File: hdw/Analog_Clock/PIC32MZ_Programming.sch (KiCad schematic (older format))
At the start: 10 parts

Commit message: a few sch adjustments
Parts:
- removed R?: 100, Resistors_SMD:R_0402, symbol Custom_Library:R_Custom
- added R?: 10, Resistors_SMD:R_0402, symbol Custom_Library:R_Custom
- R?: Digi-Key PN (none) -> 541-3964-1-ND
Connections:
- net at C?.1, R?.2, R?.2: now also R?.2
- net at Q?.3 (D): now also R?.1
- net ICSPCLK renamed PIC32MZ_ICSPCLK
- net ICSPDAT renamed PIC32MZ_ICSPDAT
- net ~MCLR renamed ~PIC32MZ_MCLR
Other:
- moved on the sheet: C?
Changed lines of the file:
@@
 encoding utf-8
 Sheet 8 20
-Title "VFD Clock"
-Date "2019-04-11"
+Title "Pulse Oximeter"
+Date "2020-08-01"
 Rev "A"
 Comp "Drew Maatman"
@@
 $EndComp
 Text GLabel 1270 1790 2    50   UnSpc ~ 0
-~MCLR
+~PIC32MZ_MCLR
 Text GLabel 1270 2090 2    50   BiDi ~ 0
-ICSPDAT
+PIC32MZ_ICSPDAT
 Text GLabel 1270 2190 2    50   Output ~ 0
-ICSPCLK
+PIC32MZ_ICSPCLK
 $Comp
 L power:GND #PWR?
 U 1 1 5BB4A7C4
-P 1790 2040
-F 0 "#PWR?" H 1790 1790 50  0001 C CNN
-F 1 "GND" H 1790 1890 50  0000 C CNN
-F 2 "" H 1790 2040 50  0001 C CNN
-F 3 "" H 1790 2040 50  0001 C CNN
-	1    1790 2040
+P 2160 2040
+F 0 "#PWR?" H 2160 1790 50  0001 C CNN
+F 1 "GND" H 2160 1890 50  0000 C CNN
+F 2 "" H 2160 2040 50  0001 C CNN
+F 3 "" H 2160 2040 50  0001 C CNN
+	1    2160 2040
 	-1   0    0    -1
 $EndComp
 Wire Wire Line
-	1790 1820 1790 1890
-Wire Wire Line
-	1790 1890 1270 1890
-Wire Wire Line
-	1790 2040 1790 1990
-Wire Wire Line
-	1790 1990 1270 1990
+	2160 1820 2160 1890
+Wire Wire Line
+	2160 2040 2160 1990
 NoConn ~ 1270 2290
 $Comp
 L Custom_Library:C_Custom C?
 U 1 1 5BC13497
-P 2460 2030
-F 0 "C?" H 2485 2130 50  0000 L CNN
-F 1 "0.1uF" H 2485 1930 50  0000 L CNN
-F 2 "Capacitors_SMD:C_0402" H 2498 1880 50  0001 C CNN
-F 3 "" H 2485 2130 50  0001 C CNN
-F 4 "0402" H 2310 2130 50  0000 R CNN "display_footprint"
-F 5 "50V" H 2310 2030 50  0000 R CNN "Voltage"
-F 6 "X7R" H 2310 1930 50  0000 R CNN "Dielectric"
-F 7 "490-10701-1-ND" H 2885 2530 60  0001 C CNN "Digi-Key PN"
-	1    2460 2030
+P 2790 2030
+F 0 "C?" H 2815 2130 50  0000 L CNN
+F 1 "0.1uF" H 2815 1930 50  0000 L CNN
+F 2 "Capacitors_SMD:C_0402" H 2828 1880 50  0001 C CNN
+F 3 "" H 2815 2130 50  0001 C CNN
+F 4 "0402" H 2640 2130 50  0000 R CNN "display_footprint"
+F 5 "50V" H 2640 2030 50  0000 R CNN "Voltage"
+F 6 "X7R" H 2640 1930 50  0000 R CNN "Dielectric"
+F 7 "490-10701-1-ND" H 3215 2530 60  0001 C CNN "Digi-Key PN"
+	1    2790 2030
 	1    0    0    -1
 $EndComp
@@
 L power:GND #PWR?
 U 1 1 5BC1349E
-P 2460 2180
-F 0 "#PWR?" H 2460 1930 50  0001 C CNN
-F 1 "GND" H 2460 2030 50  0000 C CNN
-F 2 "" H 2460 2180 50  0001 C CNN
-F 3 "" H 2460 2180 50  0001 C CNN
-	1    2460 2180
+P 2790 2180
+F 0 "#PWR?" H 2790 1930 50  0001 C CNN
+F 1 "GND" H 2790 2030 50  0000 C CNN
+F 2 "" H 2790 2180 50  0001 C CNN
+F 3 "" H 2790 2180 50  0001 C CNN
+	1    2790 2180
 	1    0    0    -1
 $EndComp
@@
 AR Path="/5CB0BC26/5BC152E5" Ref="R?"  Part="1"
 AR Path="/5E697920/5BC152E5" Ref="R?"  Part="1"
-AR Path="/5E939EAF/5BC152E5" Ref="R?"  Part="1"
+AR Path="/5EAE2EF2/5BC152E5" Ref="R?"  Part="1"
 F 0 "R?" H 7490 2020 50  0000 R CNN
 F 1 "10k" V 7550 2020 50  0000 C CNN
@@
 Connection ~ 7550 2250
 Text GLabel 8230 2250 2    50   UnSpc ~ 0
-~MCLR
+~PIC32MZ_MCLR
 $Comp
 L Switch:SW_Push SW?
@@
 	1    5020 2770
 	1    0    0    -1
-$EndComp
-$Comp
-L Custom_Library:R_Custom R?
-U 1 1 5BC190FF
-P 6860 2250
-F 0 "R?" V 6760 2250 50  0000 C CNN
-F 1 "100" V 6860 2250 50  0000 C CNN
-F 2 "Resistors_SMD:R_0402" H 6860 2250 50  0001 C CNN
-F 3 "" H 6860 2250 50  0001 C CNN
-F 4 "0402" V 6960 2250 50  0000 C CNN "display_footprint"
-F 5 "1%" V 7060 2250 50  0000 C CNN "Tolerance"
-F 6 "1/16W" V 7160 2250 50  0000 C CNN "Wattage"
-F 7 "" H 7160 2650 60  0001 C CNN "Digi-Key PN"
-	1    6860 2250
-	0    1    1    0
 $EndComp
 Wire Wire Line
@@
 F 5 "1%" V 5670 2770 50  0000 C CNN "Tolerance"
 F 6 "1/16W" V 5770 2770 50  0000 C CNN "Wattage"
-F 7 "" H 5770 3170 60  0001 C CNN "Digi-Key PN"
+F 7 "541-3964-1-ND" H 5770 3170 60  0001 C CNN "Digi-Key PN"
 	1    5470 2770
 	0    -1   -1   0
@@
 AR Path="/5CB0BC26/5BE087D6" Ref="R?"  Part="1"
 AR Path="/5E697920/5BE087D6" Ref="R?"  Part="1"
-AR Path="/5E939EAF/5BE087D6" Ref="R?"  Part="1"
+AR Path="/5EAE2EF2/5BE087D6" Ref="R?"  Part="1"
 F 0 "R?" H 5860 3000 50  0000 R CNN
 F 1 "10k" V 5920 3000 50  0000 C CNN
@@
 L power:+3.3V #PWR?
 U 1 1 5E6EC62F
-P 2460 1880
-F 0 "#PWR?" H 2460 1730 50  0001 C CNN
-F 1 "+3.3V" H 2460 2020 50  0000 C CNN
-F 2 "" H 2460 1880 50  0001 C CNN
-F 3 "" H 2460 1880 50  0001 C CNN
-	1    2460 1880
+P 2790 1880
+F 0 "#PWR?" H 2790 1730 50  0001 C CNN
+F 1 "+3.3V" H 2790 2020 50  0000 C CNN
+F 2 "" H 2790 1880 50  0001 C CNN
+F 3 "" H 2790 1880 50  0001 C CNN
+	1    2790 1880
 	1    0    0    -1
 $EndComp
@@
 L power:+3.3V #PWR?
 U 1 1 5E6ECA36
-P 1790 1820
-F 0 "#PWR?" H 1790 1670 50  0001 C CNN
-F 1 "+3.3V" H 1790 1960 50  0000 C CNN
-F 2 "" H 1790 1820 50  0001 C CNN
-F 3 "" H 1790 1820 50  0001 C CNN
-	1    1790 1820
+P 2160 1820
+F 0 "#PWR?" H 2160 1670 50  0001 C CNN
+F 1 "+3.3V" H 2160 1960 50  0000 C CNN
+F 2 "" H 2160 1820 50  0001 C CNN
+F 3 "" H 2160 1820 50  0001 C CNN
+	1    2160 1820
 	1    0    0    -1
 $EndComp
@@
 	1    0    0    -1
 $EndComp
+Wire Wire Line
+	1270 1890 2160 1890
+Wire Wire Line
+	1270 1990 2160 1990
+$Comp
+L Custom_Library:R_Custom R?
+U 1 1 5EB9A4D9
+P 6860 2250
+F 0 "R?" V 6760 2250 50  0000 C CNN
+F 1 "10" V 6860 2250 50  0000 C CNN
+F 2 "Resistors_SMD:R_0402" H 6860 2250 50  0001 C CNN
+F 3 "" H 6860 2250 50  0001 C CNN
+F 4 "0402" V 6960 2250 50  0000 C CNN "display_footprint"
+F 5 "1%" V 7060 2250 50  0000 C CNN "Tolerance"
+F 6 "1/16W" V 7160 2250 50  0000 C CNN "Wattage"
+F 7 "541-3964-1-ND" H 7160 2650 60  0001 C CNN "Digi-Key PN"
+	1    6860 2250
+	0    -1   -1   0
+$EndComp
 $EndSCHEMATC

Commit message: more analog work, added some more sch stuff
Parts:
- removed J?: PICKIT3, Custom Footprints Library:PICKIT3_Header, symbol Connector_Generic:Conn_01x06
- added D? (x5): PESD3V3L5UY, Package_TO_SOT_SMD:SOT-363_SC-70-6, symbol Power_Protection:PESD3V3L5UY
- added J?: PICKIT4, Custom Footprints Library:PICKIT4_Header, symbol Connector_Generic:Conn_01x08
- added L? (x2): 600R 0.5A, Inductors_SMD:L_0402, symbol Device:Ferrite_Bead
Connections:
- net +3V3: now also D?.3 (K2), J?.2 (Pin_2)
- net GND: now also D?.2 (A), L?.2
- net PIC32MZ_ICSPCLK: now also D?.5 (K4), J?.5 (Pin_5)
- net PIC32MZ_ICSPDAT: now also D?.4 (K3), J?.4 (Pin_4)
- net ~PIC32MZ_MCLR: now also L?.1
- new net: D?.1 (K1), J?.1 (Pin_1), L?.2
- new net: J?.3 (Pin_3), L?.1
- no-connect marks 1 -> 4
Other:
- moved on the sheet: C?, Q?, R?, SW?

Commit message: big sch push
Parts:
- C801, C802: renamed from C?; footprint Capacitors_SMD:C_0402 -> Capacitors_SMD:C_0603; Digi-Key PN 490-10701-1-ND -> 399-7845-1-ND; display_footprint 0402 -> 0603
- D801: renamed from D?; Digi-Key PN (none) -> 1727-3828-1-ND
- L801, L802: renamed from L?; footprint Inductors_SMD:L_0402 -> Inductors_SMD:L_0603; Digi-Key PN 490-5441-1-ND -> 732-1593-1-ND
- R801, R803: renamed from R?; footprint Resistors_SMD:R_0402 -> Resistors_SMD:R_0603; Digi-Key PN 541-3964-1-ND -> (none); Wattage 1/16W -> 1/10W; display_footprint 0402 -> 0603
- R802, R804: renamed from R?; footprint Resistors_SMD:R_0402 -> Resistors_SMD:R_0603; Digi-Key PN RMCF0402FT10K0CT-ND -> (none); Wattage 1/16W -> 1/10W; display_footprint 0402 -> 0603
- R805: renamed from R?; footprint Resistors_SMD:R_0402 -> Resistors_SMD:R_0603; Digi-Key PN 541-1.00KLCT-ND -> (none); Wattage 1/16W -> 1/10W; display_footprint 0402 -> 0603
- gave numbers to parts that had none: 3

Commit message: Much more schematic progress
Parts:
- R801, R802, R803, R804: Digi-Key PN (none) -> YAG2321CT-ND
- R805: Digi-Key PN (none) -> 311-1.00KHRCT-ND
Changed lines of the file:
@@
 encoding utf-8
 Sheet 8 25
-Title "Pulse Oximeter"
-Date "2020-08-01"
+Title "Analog Clock"
+Date "2020-08-15"
 Rev "A"
 Comp "Drew Maatman"
@@
 F 5 "1%" H 5950 4770 50  0000 C CNN "Tolerance"
 F 6 "1/10W" H 5980 4700 50  0000 C CNN "Wattage"
-F 7 "" H 6070 5170 60  0001 C CNN "Digi-Key PN"
+F 7 "YAG2321CT-ND" H 6070 5170 60  0001 C CNN "Digi-Key PN"
 	1    5770 4770
 	-1   0    0    -1
@@
 F 5 "1%" V 6500 5000 50  0000 C CNN "Tolerance"
 F 6 "1/10W" V 6600 5000 50  0000 C CNN "Wattage"
-F 7 "" H 6600 5400 60  0001 C CNN "Digi-Key PN"
+F 7 "311-1.00KHRCT-ND" H 6600 5400 60  0001 C CNN "Digi-Key PN"
 	1    6300 5000
 	0    1    1    0
@@
 F 5 "1%" V 3890 5520 50  0000 C CNN "Tolerance"
 F 6 "1/10W" V 3990 5520 50  0000 C CNN "Wattage"
-F 7 "" H 3990 5920 60  0001 C CNN "Digi-Key PN"
+F 7 "YAG2321CT-ND" H 3990 5920 60  0001 C CNN "Digi-Key PN"
 	1    3690 5520
 	0    -1   -1   0
@@
 F 5 "1%" H 4320 5750 50  0000 C CNN "Tolerance"
 F 6 "1/10W" H 4350 5680 50  0000 C CNN "Wattage"
-F 7 "" H 4440 6150 60  0001 C CNN "Digi-Key PN"
+F 7 "YAG2321CT-ND" H 4440 6150 60  0001 C CNN "Digi-Key PN"
 	1    4140 5750
 	1    0    0    -1
@@
 F 5 "1%" V 5280 5000 50  0000 C CNN "Tolerance"
 F 6 "1/10W" V 5380 5000 50  0000 C CNN "Wattage"
-F 7 "" H 5380 5400 60  0001 C CNN "Digi-Key PN"
+F 7 "YAG2321CT-ND" H 5380 5400 60  0001 C CNN "Digi-Key PN"
 	1    5080 5000
 	0    -1   -1   0

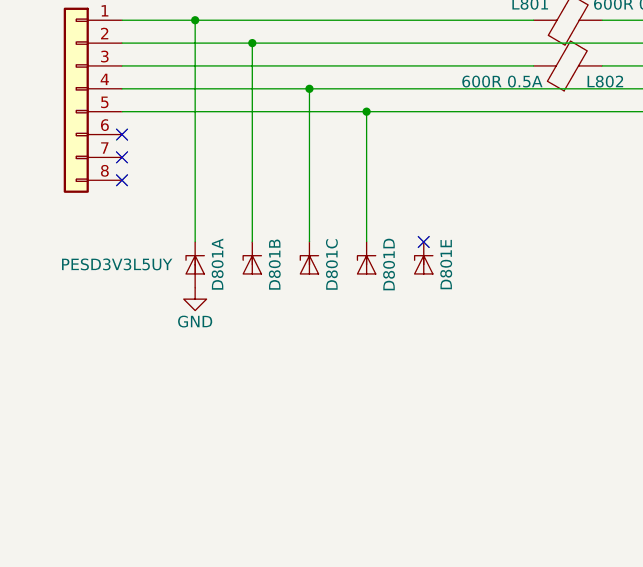
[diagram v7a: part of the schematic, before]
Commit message: more PCB grouping
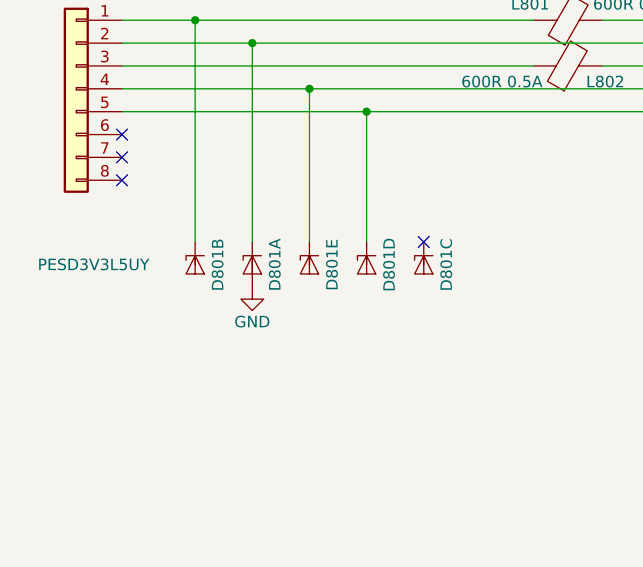
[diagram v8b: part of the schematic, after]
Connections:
- net +3V3: now also D801.1 (K1); no longer D801.3 (K2)
- net PIC32MZ_ICSPDAT: now also D801.6 (K5); no longer D801.4 (K3)
- net at J801.1 (Pin_1), L801.2: now also D801.3 (K2); no longer D801.1 (K1)
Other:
- moved on the sheet: D801A, D801B, D801C, D801E
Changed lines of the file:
@@
 L Power_Protection:PESD3V3L5UY D801
 U 1 1 5F37FACB
-P 3490 2930
-F 0 "D801" H 3490 3030 50  0000 C CNN
-F 1 "PESD3V3L5UY" V 3490 2830 50  0000 R CNN
-F 2 "Package_TO_SOT_SMD:SOT-363_SC-70-6" H 3490 2930 50  0001 C CNN
-F 3 "https://assets.nexperia.com/documents/data-sheet/PESDXL5UF_V_Y.pdf" H 3490 2930 50  0001 C CNN
-F 4 "1727-3828-1-ND" H 3490 2930 50  0001 C CNN "Digi-Key PN"
-	1    3490 2930
-	0    1    1    0
-$EndComp
-$Comp
-L Power_Protection:PESD3V3L5UY D801
-U 2 1 5F38087E
 P 3740 2930
 F 0 "D801" H 3740 3030 50  0000 C CNN
-F 1 "PESD3V3L5UY" H 3740 2830 50  0001 C CNN
+F 1 "PESD3V3L5UY" V 3740 2480 50  0000 R CNN
 F 2 "Package_TO_SOT_SMD:SOT-363_SC-70-6" H 3740 2930 50  0001 C CNN
 F 3 "https://assets.nexperia.com/documents/data-sheet/PESDXL5UF_V_Y.pdf" H 3740 2930 50  0001 C CNN
 F 4 "1727-3828-1-ND" H 3740 2930 50  0001 C CNN "Digi-Key PN"
-	2    3740 2930
+	1    3740 2930
 	0    1    1    0
 $EndComp
@@
 L Power_Protection:PESD3V3L5UY D801
 U 3 1 5F380F72
-P 3990 2930
-F 0 "D801" H 3990 3030 50  0000 C CNN
-F 1 "PESD3V3L5UY" H 3990 2830 50  0001 C CNN
-F 2 "Package_TO_SOT_SMD:SOT-363_SC-70-6" H 3990 2930 50  0001 C CNN
-F 3 "https://assets.nexperia.com/documents/data-sheet/PESDXL5UF_V_Y.pdf" H 3990 2930 50  0001 C CNN
-F 4 "1727-3828-1-ND" H 3990 2930 50  0001 C CNN "Digi-Key PN"
-	3    3990 2930
+P 4490 2930
+F 0 "D801" H 4490 3030 50  0000 C CNN
+F 1 "PESD3V3L5UY" H 4490 2830 50  0001 C CNN
+F 2 "Package_TO_SOT_SMD:SOT-363_SC-70-6" H 4490 2930 50  0001 C CNN
+F 3 "https://assets.nexperia.com/documents/data-sheet/PESDXL5UF_V_Y.pdf" H 4490 2930 50  0001 C CNN
+F 4 "1727-3828-1-ND" H 4490 2930 50  0001 C CNN "Digi-Key PN"
+	3    4490 2930
 	0    1    1    0
 $EndComp
@@
 L power:GND #PWR0802
 U 1 1 5F3831ED
-P 3490 3030
-F 0 "#PWR0802" H 3490 2780 50  0001 C CNN
-F 1 "GND" H 3490 2880 50  0000 C CNN
-F 2 "" H 3490 3030 50  0001 C CNN
-F 3 "" H 3490 3030 50  0001 C CNN
-	1    3490 3030
-	1    0    0    -1
+P 3740 3030
+F 0 "#PWR0802" H 3740 2780 50  0001 C CNN
+F 1 "GND" H 3740 2880 50  0000 C CNN
+F 2 "" H 3740 3030 50  0001 C CNN
+F 3 "" H 3740 3030 50  0001 C CNN
+	1    3740 3030
+	-1   0    0    -1
 $EndComp
 $Comp
@@
 Wire Wire Line
 	4240 2260 3170 2260
-$Comp
-L Power_Protection:PESD3V3L5UY D801
-U 5 1 5F39050C
-P 4490 2930
-F 0 "D801" H 4490 3030 50  0000 C CNN
-F 1 "PESD3V3L5UY" H 4490 2830 50  0001 C CNN
-F 2 "Package_TO_SOT_SMD:SOT-363_SC-70-6" H 4490 2930 50  0001 C CNN
-F 3 "https://assets.nexperia.com/documents/data-sheet/PESDXL5UF_V_Y.pdf" H 4490 2930 50  0001 C CNN
-F 4 "1727-3828-1-ND" H 4490 2930 50  0001 C CNN "Digi-Key PN"
-	5    4490 2930
-	0    1    1    0
-$EndComp
 NoConn ~ 4490 2830
 Wire Wire Line
@@
 	0    -1   -1   0
 $EndComp
+$Comp
+L Power_Protection:PESD3V3L5UY D801
+U 5 1 5F39050C
+P 3990 2930
+F 0 "D801" H 3990 3030 50  0000 C CNN
+F 1 "PESD3V3L5UY" H 3990 2830 50  0001 C CNN
+F 2 "Package_TO_SOT_SMD:SOT-363_SC-70-6" H 3990 2930 50  0001 C CNN
+F 3 "https://assets.nexperia.com/documents/data-sheet/PESDXL5UF_V_Y.pdf" H 3990 2930 50  0001 C CNN
+F 4 "1727-3828-1-ND" H 3990 2930 50  0001 C CNN "Digi-Key PN"
+	5    3990 2930
+	0    1    1    0
+$EndComp
+$Comp
+L Power_Protection:PESD3V3L5UY D801
+U 2 1 5F38087E
+P 3490 2930
+F 0 "D801" H 3490 3030 50  0000 C CNN
+F 1 "PESD3V3L5UY" H 3490 2830 50  0001 C CNN
+F 2 "Package_TO_SOT_SMD:SOT-363_SC-70-6" H 3490 2930 50  0001 C CNN
+F 3 "https://assets.nexperia.com/documents/data-sheet/PESDXL5UF_V_Y.pdf" H 3490 2930 50  0001 C CNN
+F 4 "1727-3828-1-ND" H 3490 2930 50  0001 C CNN "Digi-Key PN"
+	2    3490 2930
+	0    1    1    0
+$EndComp
 $EndSCHEMATC
